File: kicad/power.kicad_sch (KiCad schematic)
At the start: 13 parts, among them J12 Barrel_Jack, U4 TPS62142, U5 LP5907MFX-3.0

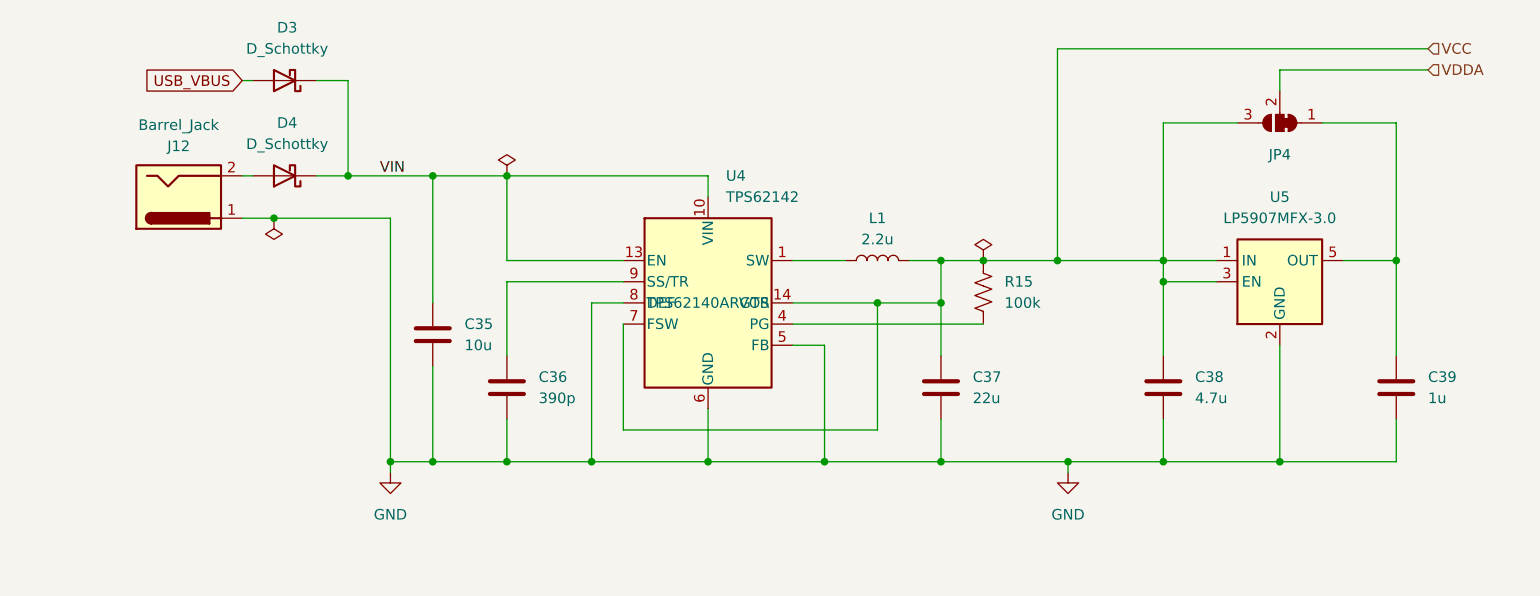
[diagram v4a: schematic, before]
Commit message: Finish part sourcing and start PCB layout
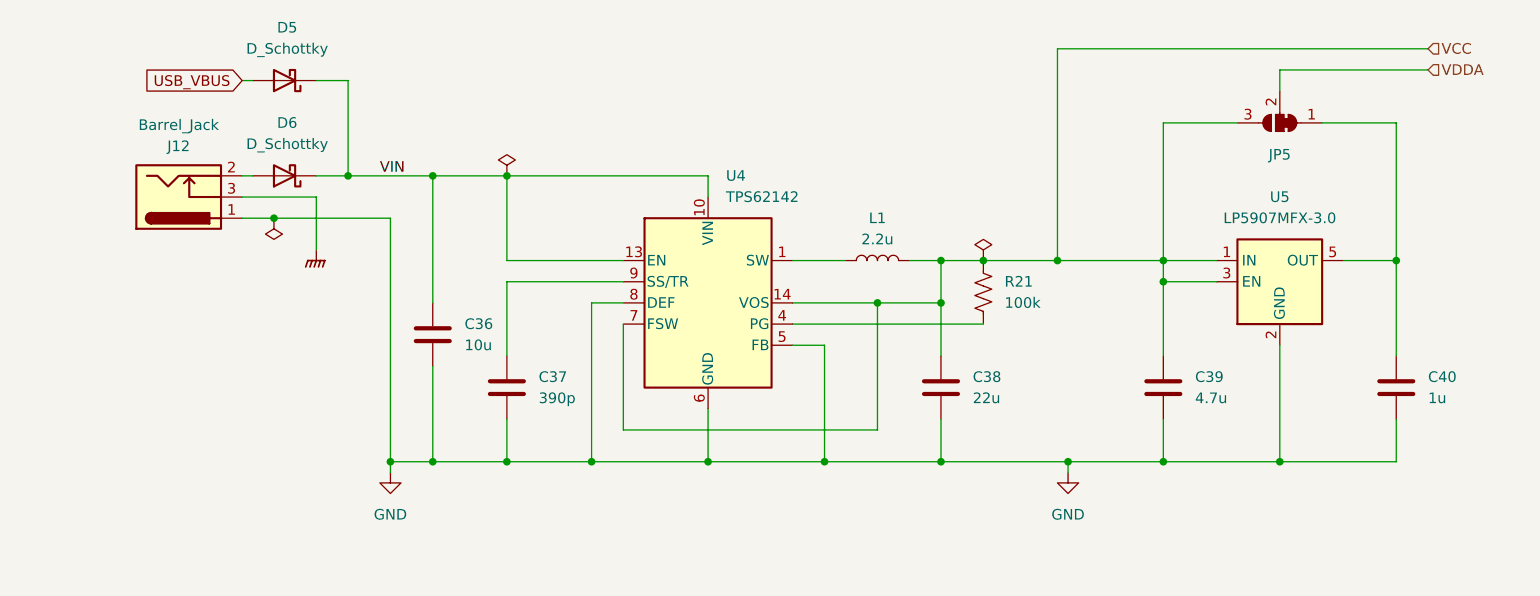
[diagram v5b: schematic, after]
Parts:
- J12: footprint SameSky:CUI_PJ-002A -> SameSky:PJ002AHSMTTR; symbol Connector:Barrel_Jack -> Connector:Barrel_Jack_Switch; Part (none) -> PJ-002AH-SMT-TR
- JP5: renamed from JP4; footprint (none) -> Jumper:SolderJumper-3_P1.3mm_Bridged12_Pad1.0x1.5mm
- renumbered C35 to C36, C36 to C37, C37 to C38, C38 to C39, C39 to C40, D3 to D5, D4 to D6, R15 to R21
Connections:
- new net GNDPWR: J12.3
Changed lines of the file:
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@@
+	(wire
+		(pts
+			(xy 78.74 91.44) (xy 87.63 91.44)
+		)
+		(stroke
+			(width 0)
+			(type default)
+		)
+	)
 	(wire
 		(pts
@@
 		(pts
 			(xy 217.17 82.55) (xy 217.17 99.06)
+		)
+		(stroke
+			(width 0)
+			(type default)
+		)
+	)
+	(wire
+		(pts
+			(xy 87.63 91.44) (xy 87.63 97.79)
 		)
 		(stroke
@@
 		(dnp no)
 		(fields_autoplaced yes)
-		(property "Reference" "C38"
+		(property "Reference" "C39"
 			(at 193.04 113.0299 0)
 			(effects
@@
 			(project ""
 				(path "/79bfec23-3e7b-4837-8996-6bbe67be3d6b/50d1ea01-1e05-4a9c-ae07-2b1d5c2735d5"
-					(reference "C38")
+					(reference "C39")
 					(unit 1)
 				)
@@
 		(dnp no)
 		(fields_autoplaced yes)
-		(property "Reference" "C39"
+		(property "Reference" "C40"
 			(at 220.98 113.0299 0)
 			(effects
@@
 			(project ""
 				(path "/79bfec23-3e7b-4837-8996-6bbe67be3d6b/50d1ea01-1e05-4a9c-ae07-2b1d5c2735d5"
-					(reference "C39")
+					(reference "C40")
 					(unit 1)
 				)
@@
 					(size 1.27 1.27)
 				)
+				(hide yes)
 			)
 		)
@@
 		(dnp no)
 		(fields_autoplaced yes)
-		(property "Reference" "D3"
+		(property "Reference" "D5"
 			(at 84.1375 71.12 0)
 			(effects
@@
 			(project ""
 				(path "/79bfec23-3e7b-4837-8996-6bbe67be3d6b/50d1ea01-1e05-4a9c-ae07-2b1d5c2735d5"
-					(reference "D3")
+					(reference "D5")
 					(unit 1)
 				)
@@
 	)
 	(symbol
-		(lib_id "Connector:Barrel_Jack")
+		(lib_id "Connector:Barrel_Jack_Switch")
 		(at 71.12 91.44 0)
 		(mirror x)
@@
 			)
 		)
-		(property "Footprint" "SameSky:CUI_PJ-002A"
+		(property "Footprint" "SameSky:PJ002AHSMTTR"
 			(at 72.39 90.424 0)
 			(effects
@@
 			)
 		)
-		(property "Datasheet" "~"
+		(property "Datasheet" "https://www.mouser.com/datasheet/3/6118/1/pj_002ah_smt_tr.pdf"
 			(at 72.39 90.424 0)
 			(effects
@@
 			)
 		)
-		(property "Description" "DC Barrel Jack"
+		(property "Description" "DC Barrel Jack with an internal switch"
 			(at 71.12 91.44 0)
 			(effects
@@
 			)
 		)
-		(property "Part" ""
+		(property "Part" "PJ-002AH-SMT-TR"
 			(at 71.12 91.44 0)
 			(effects
@@
 		)
 		(pin "2"
+		)
+		(pin "3"
 		)
 		(instances
@@
 		(on_board yes)
 		(dnp no)
-		(property "Reference" "JP4"
+		(property "Reference" "JP5"
 			(at 203.2 86.36 0)
 			(effects
@@
 			)
 		)
-		(property "Footprint" ""
+		(property "Footprint" "Jumper:SolderJumper-3_P1.3mm_Bridged12_Pad1.0x1.5mm"
 			(at 203.2 82.55 0)
 			(effects
@@
 			(project ""
 				(path "/79bfec23-3e7b-4837-8996-6bbe67be3d6b/50d1ea01-1e05-4a9c-ae07-2b1d5c2735d5"
-					(reference "JP4")
+					(reference "JP5")
 					(unit 1)
 				)
@@
 		(dnp no)
 		(fields_autoplaced yes)
-		(property "Reference" "#PWR044"
+		(property "Reference" "#PWR053"
 			(at 96.52 130.81 0)
 			(effects
@@
 			(project ""
 				(path "/79bfec23-3e7b-4837-8996-6bbe67be3d6b/50d1ea01-1e05-4a9c-ae07-2b1d5c2735d5"
-					(reference "#PWR044")
+					(reference "#PWR053")
 					(unit 1)
 				)
@@
 		(dnp no)
 		(fields_autoplaced yes)
-		(property "Reference" "#PWR045"
+		(property "Reference" "#PWR054"
 			(at 177.8 130.81 0)
 			(effects
@@
 			(project ""
 				(path "/79bfec23-3e7b-4837-8996-6bbe67be3d6b/50d1ea01-1e05-4a9c-ae07-2b1d5c2735d5"
-					(reference "#PWR045")
+					(reference "#PWR054")
 					(unit 1)
 				)
@@
 		(dnp no)
 		(fields_autoplaced yes)
-		(property "Reference" "#FLG04"
+		(property "Reference" "#FLG05"
 			(at 110.49 86.995 0)
 			(effects
@@
 			(project "effect-pedal"
 				(path "/79bfec23-3e7b-4837-8996-6bbe67be3d6b/50d1ea01-1e05-4a9c-ae07-2b1d5c2735d5"
-					(reference "#FLG04")
+					(reference "#FLG05")
 					(unit 1)
 				)
@@
 		(dnp no)
 		(fields_autoplaced yes)
-		(property "Reference" "C37"
+		(property "Reference" "C38"
 			(at 166.37 113.0299 0)
 			(effects
@@
 			(project ""
 				(path "/79bfec23-3e7b-4837-8996-6bbe67be3d6b/50d1ea01-1e05-4a9c-ae07-2b1d5c2735d5"
-					(reference "C37")
+					(reference "C38")
 					(unit 1)
 				)
@@
 		(on_board yes)
 		(dnp no)
-		(property "Reference" "#FLG03"
+		(property "Reference" "#FLG04"
 			(at 82.55 95.885 0)
 			(effects
@@
 			(project "effect-pedal"
 				(path "/79bfec23-3e7b-4837-8996-6bbe67be3d6b/50d1ea01-1e05-4a9c-ae07-2b1d5c2735d5"
-					(reference "#FLG03")
+					(reference "#FLG04")
 					(unit 1)
 				)
@@
 		(dnp no)
 		(fields_autoplaced yes)
-		(property "Reference" "R15"
+		(property "Reference" "R21"
 			(at 170.18 101.5999 0)
 			(effects
@@
 			(project ""
 				(path "/79bfec23-3e7b-4837-8996-6bbe67be3d6b/50d1ea01-1e05-4a9c-ae07-2b1d5c2735d5"
-					(reference "R15")
+					(reference "R21")
+					(unit 1)
+				)
+			)
+		)
+	)
+	(symbol
+		(lib_id "power:GNDPWR")
+		(at 87.63 97.79 0)
+		(unit 1)
+		(exclude_from_sim no)
+		(in_bom yes)
+		(on_board yes)
+		(dnp no)
+		(fields_autoplaced yes)
+		(property "Reference" "#PWR052"
+			(at 87.63 102.87 0)
+			(effects
+				(font
+					(size 1.27 1.27)
+				)
+				(hide yes)
+			)
+		)
+		(property "Value" "GNDPWR"
+			(at 87.503 101.6 0)
+			(effects
+				(font
+					(size 1.27 1.27)
+				)
+				(hide yes)
+			)
+		)
+		(property "Footprint" ""
+			(at 87.63 99.06 0)
+			(effects
+				(font
+					(size 1.27 1.27)
+				)
+				(hide yes)
+			)
+		)
+		(property "Datasheet" ""
+			(at 87.63 99.06 0)
+			(effects
+				(font
+					(size 1.27 1.27)
+				)
+				(hide yes)
+			)
+		)
+		(property "Description" "Power symbol creates a global label with name \"GNDPWR\" , global ground"
+			(at 87.63 97.79 0)
+			(effects
+				(font
+					(size 1.27 1.27)
+				)
+				(hide yes)
+			)
+		)
+		(pin "1"
+		)
+		(instances
+			(project ""
+				(path "/79bfec23-3e7b-4837-8996-6bbe67be3d6b/50d1ea01-1e05-4a9c-ae07-2b1d5c2735d5"
+					(reference "#PWR052")
 					(unit 1)
 				)
@@
 		(dnp no)
 		(fields_autoplaced yes)
-		(property "Reference" "C35"
+		(property "Reference" "C36"
 			(at 105.41 106.6799 0)
 			(effects
@@
 			(project ""
 				(path "/79bfec23-3e7b-4837-8996-6bbe67be3d6b/50d1ea01-1e05-4a9c-ae07-2b1d5c2735d5"
-					(reference "C35")
+					(reference "C36")
 					(unit 1)
 				)
@@
 		(dnp no)
 		(fields_autoplaced yes)
-		(property "Reference" "C36"
+		(property "Reference" "C37"
 			(at 114.3 113.0299 0)
 			(effects
@@
 			(project ""
 				(path "/79bfec23-3e7b-4837-8996-6bbe67be3d6b/50d1ea01-1e05-4a9c-ae07-2b1d5c2735d5"
-					(reference "C36")
+					(reference "C37")
 					(unit 1)
 				)
@@
 		(dnp no)
 		(fields_autoplaced yes)
-		(property "Reference" "#FLG05"
+		(property "Reference" "#FLG06"
 			(at 167.64 97.155 0)
 			(effects
@@
 			(project ""
 				(path "/79bfec23-3e7b-4837-8996-6bbe67be3d6b/50d1ea01-1e05-4a9c-ae07-2b1d5c2735d5"
-					(reference "#FLG05")
+					(reference "#FLG06")
 					(unit 1)
 				)
@@
 		(dnp no)
 		(fields_autoplaced yes)
-		(property "Reference" "D4"
+		(property "Reference" "D6"
 			(at 84.1375 82.55 0)
 			(effects
@@
 			(project "effect-pedal"
 				(path "/79bfec23-3e7b-4837-8996-6bbe67be3d6b/50d1ea01-1e05-4a9c-ae07-2b1d5c2735d5"
-					(reference "D4")
-					(unit 1)
-				)
+					(reference "D6")
+					(unit 1)
+				)

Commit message: Finish schematic
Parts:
- J12: footprint SameSky:PJ002AHSMTTR -> Custom:CUI_PJ-002AH-SMT-TR
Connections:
- net PWR_LDO_OUT: now reaches C40.1, JP5.1 (A), U5.5 (OUT)
- net PWR_SW: now reaches L1.1, U4.1 (SW), U4.2 (SW), U4.3 (SW)
- net PG: now reaches R21.2, U4.4 (PG)
- net SS: now reaches C37.1, U4.9 (SS/TR)
- net VIN_JACK: now reaches D6.2 (A), J12.2
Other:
- moved on the sheet: J12, L1
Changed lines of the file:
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@@
 	(wire
 		(pts
-			(xy 78.74 91.44) (xy 87.63 91.44)
+			(xy 67.31 91.44) (xy 87.63 91.44)
 		)
 		(stroke
@@
 	(wire
 		(pts
-			(xy 78.74 93.98) (xy 82.55 93.98)
+			(xy 67.31 93.98) (xy 82.55 93.98)
 		)
 		(stroke
@@
 	(wire
 		(pts
-			(xy 144.78 99.06) (xy 151.13 99.06)
+			(xy 144.78 99.06) (xy 153.67 99.06)
 		)
 		(stroke
@@
 	(wire
 		(pts
+			(xy 217.17 99.06) (xy 232.41 99.06)
+		)
+		(stroke
+			(width 0)
+			(type default)
+		)
+	)
+	(wire
+		(pts
 			(xy 162.56 104.14) (xy 162.56 110.49)
 		)
@@
 	(wire
 		(pts
-			(xy 78.74 77.47) (xy 80.01 77.47)
-		)
-		(stroke
-			(width 0)
-			(type default)
-		)
-	)
-	(wire
-		(pts
-			(xy 158.75 99.06) (xy 162.56 99.06)
+			(xy 66.04 77.47) (xy 80.01 77.47)
+		)
+		(stroke
+			(width 0)
+			(type default)
+		)
+	)
+	(wire
+		(pts
+			(xy 161.29 99.06) (xy 162.56 99.06)
 		)
 		(stroke
@@
 	(wire
 		(pts
-			(xy 78.74 88.9) (xy 80.01 88.9)
+			(xy 67.31 88.9) (xy 80.01 88.9)
 		)
 		(stroke
@@
 			(width 0)
 			(type default)
+		)
+	)
+	(label "SS"
+		(at 110.49 101.6 0)
+		(effects
+			(font
+				(size 1.27 1.27)
+			)
+			(justify left bottom)
+		)
+	)
+	(label "VIN_JACK"
+		(at 69.85 88.9 0)
+		(effects
+			(font
+				(size 1.27 1.27)
+			)
+			(justify left bottom)
+		)
+	)
+	(label "PWR_SW"
+		(at 144.78 99.06 0)
+		(effects
+			(font
+				(size 1.27 1.27)
+			)
+			(justify left bottom)
 		)
 	)
@@
 		)
 	)
+	(label "PWR_LDO_OUT"
+		(at 232.41 99.06 180)
+		(effects
+			(font
+				(size 1.27 1.27)
+			)
+			(justify right bottom)
+		)
+	)
+	(label "PG"
+		(at 144.78 106.68 0)
+		(effects
+			(font
+				(size 1.27 1.27)
+			)
+			(justify left bottom)
+		)
+	)
 	(global_label "USB_VBUS"
 		(shape input)
-		(at 78.74 77.47 180)
+		(at 66.04 77.47 180)
 		(fields_autoplaced yes)
 		(effects
@@
 		)
 		(property "Intersheetrefs" "${INTERSHEET_REFS}"
-			(at 66.0786 77.47 0)
+			(at 53.3786 77.47 0)
 			(effects
 				(font
@@
 	(symbol
 		(lib_id "Connector:Barrel_Jack_Switch")
-		(at 71.12 91.44 0)
+		(at 59.69 91.44 0)
 		(mirror x)
 		(unit 1)
@@
 		(dnp no)
 		(property "Reference" "J12"
-			(at 71.12 85.344 0)
+			(at 59.69 85.344 0)
 			(effects
 				(font
@@
 		)
 		(property "Value" "Barrel_Jack"
-			(at 71.12 82.804 0)
-			(effects
-				(font
-					(size 1.27 1.27)
-				)
-			)
-		)
-		(property "Footprint" "SameSky:PJ002AHSMTTR"
-			(at 72.39 90.424 0)
+			(at 59.69 82.804 0)
+			(effects
+				(font
+					(size 1.27 1.27)
+				)
+			)
+		)
+		(property "Footprint" "Custom:CUI_PJ-002AH-SMT-TR"
+			(at 60.96 90.424 0)
 			(effects
 				(font
@@
 		)
 		(property "Datasheet" "https://www.mouser.com/datasheet/3/6118/1/pj_002ah_smt_tr.pdf"
-			(at 72.39 90.424 0)
+			(at 60.96 90.424 0)
 			(effects
 				(font
@@
 		)
 		(property "Description" "DC Barrel Jack with an internal switch"
-			(at 71.12 91.44 0)
+			(at 59.69 91.44 0)
 			(effects
 				(font
@@
 		)
 		(property "Part" "PJ-002AH-SMT-TR"
-			(at 71.12 91.44 0)
+			(at 59.69 91.44 0)
 			(effects
 				(font
@@
 	(symbol
 		(lib_id "Device:L")
-		(at 154.94 99.06 90)
+		(at 157.48 99.06 90)
 		(unit 1)
 		(exclude_from_sim no)
@@
 		(fields_autoplaced yes)
 		(property "Reference" "L1"
-			(at 154.94 93.98 90)
+			(at 157.48 93.98 90)
 			(effects
 				(font
@@
 		)
 		(property "Value" "2.2u"
-			(at 154.94 96.52 90)
+			(at 157.48 96.52 90)
 			(effects
 				(font
@@
 		)
 		(property "Footprint" "Inductor_SMD:L_Vishay_IHLP-1212"
-			(at 154.94 99.06 0)
+			(at 157.48 99.06 0)
 			(effects
 				(font
@@
 		)
 		(property "Datasheet" "https://static6.arrow.com/aropdfconversion/e61ca248c29f222088e35e1929f9b032fcf99ef/ihlp1212bz11.pdf"
-			(at 154.94 99.06 0)
+			(at 157.48 99.06 0)
 			(effects
 				(font
@@
 		)
 		(property "Description" "Inductor"
-			(at 154.94 99.06 0)
+			(at 157.48 99.06 0)
 			(effects
 				(font
@@
 		)
 		(property "Part" "IHLP1212BZEV2R2M11"
-			(at 154.94 99.06 90)
-			(effects
-				(font
+			(at 157.48 99.06 90)
+			(effects
+				(font

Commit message: Setup for production
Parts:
- U4: footprint Package_DFN_QFN:VQFN-16-1EP_3x3mm_P0.5mm_EP1.68x1.68mm_ThermalVias -> Custom:VQFN-16-1EP_3x3mm_P0.5mm_EP1.68x1.68mm_ThermalVias; Part TPS62140ARGTR -> TPS62142RGTR
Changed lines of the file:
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@@
 			)
 		)
-		(property "Footprint" "Package_DFN_QFN:VQFN-16-1EP_3x3mm_P0.5mm_EP1.68x1.68mm_ThermalVias"
+		(property "Footprint" "Custom:VQFN-16-1EP_3x3mm_P0.5mm_EP1.68x1.68mm_ThermalVias"
 			(at 138.43 115.57 0)
 			(effects
@@
 			)
 		)
-		(property "Part" "TPS62140ARGTR"
+		(property "Part" "TPS62142RGTR"
 			(at 134.62 104.14 0)
 			(effects

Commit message: Add ibom
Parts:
- C36: Part LMK107BBJ106KALT -> Generic
- C40: Part JMK107BJ105KAHT -> Generic
- L1: Part IHLP1212BZEV2R2M11 -> MPX1D1250L2R2
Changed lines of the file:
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@@
 			)
 		)
-		(property "Part" "JMK107BJ105KAHT"
+		(property "Part" "Generic"
 			(at 217.17 114.3 0)
 			(effects
@@
 			)
 		)
-		(property "Part" "IHLP1212BZEV2R2M11"
+		(property "Part" "MPX1D1250L2R2"
 			(at 157.48 99.06 90)
 			(effects
@@
 			)
 		)
-		(property "Part" "LMK107BBJ106KALT"
+		(property "Part" "Generic"
 			(at 101.6 107.95 0)
 			(effects
